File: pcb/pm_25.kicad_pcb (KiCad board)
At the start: 2 copper layers, 52.3 x 36.8 mm, 7 parts, among them J1 USB_B_Mini, U1 LD1117S33TR_TO220, U2 SI7021, U3 ESP-01v090, U4 Plantower-PM2.5

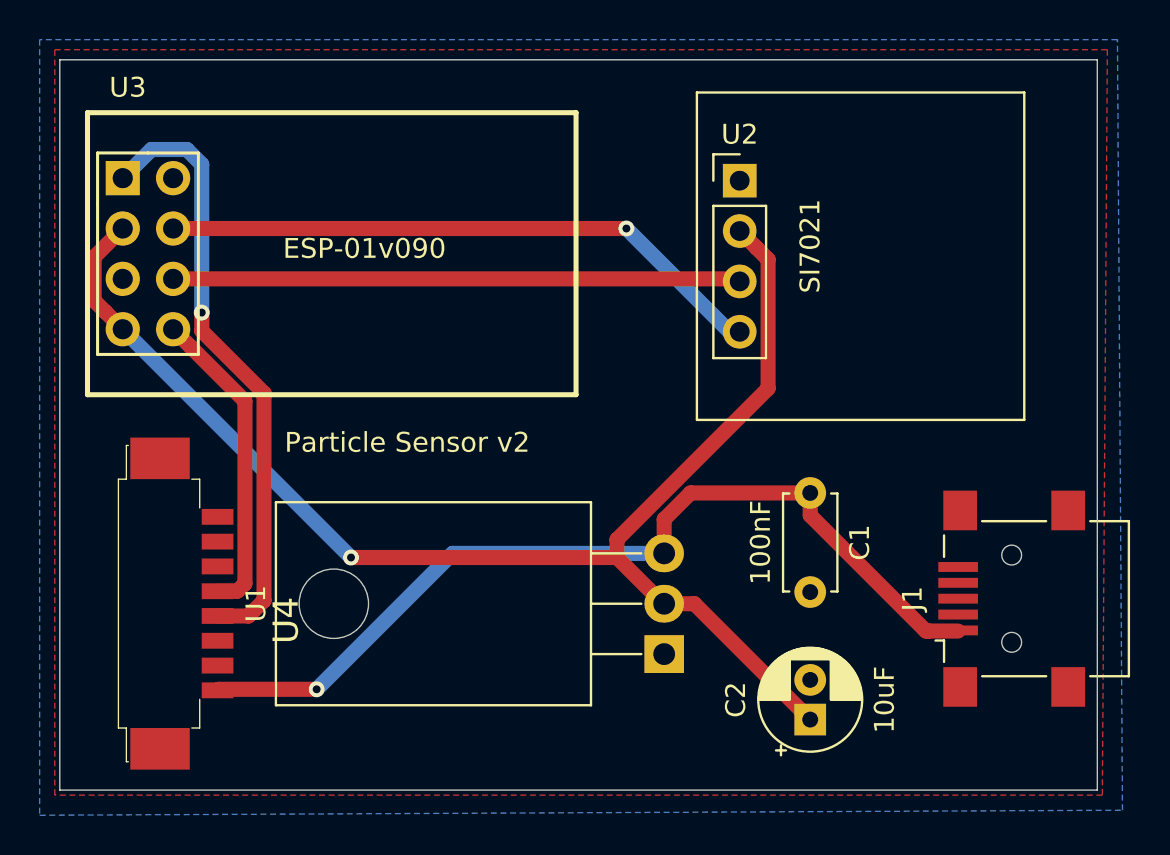
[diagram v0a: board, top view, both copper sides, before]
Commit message: make the PCB the same size as the plantower sensor
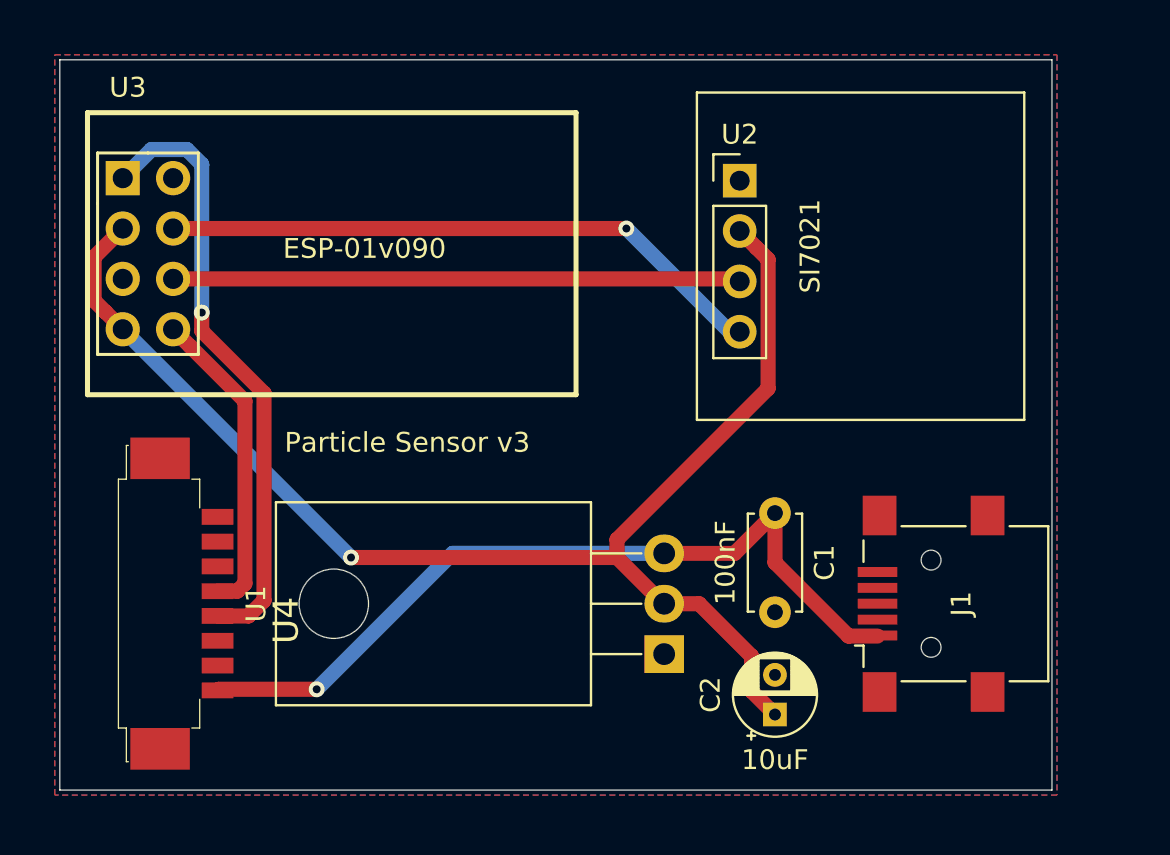
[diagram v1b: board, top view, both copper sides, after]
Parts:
- C2: footprint Capacitor_THT:CP_Radial_D5.0mm_P2.00mm -> Capacitor_THT:CP_Radial_D4.0mm_P2.00mm
- J1: value USB_B_Mini -> USB_B_Micro
- moved J1 4.07 mm to (181.1, 131.6)
- moved C1 2.05 mm to (173.2, 127.0)
- moved C2 1.80 mm to (173.2, 137.2)
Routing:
- net +5V: track 46.0 -> 41.0 mm
- net +3V3: track 69.3 -> 68.5 mm
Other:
- board size 52.3 x 36.8 mm -> 50 x 36.8 mm
- board text added: "Particle Sensor v3"
- board text removed: "Particle Sensor v2"

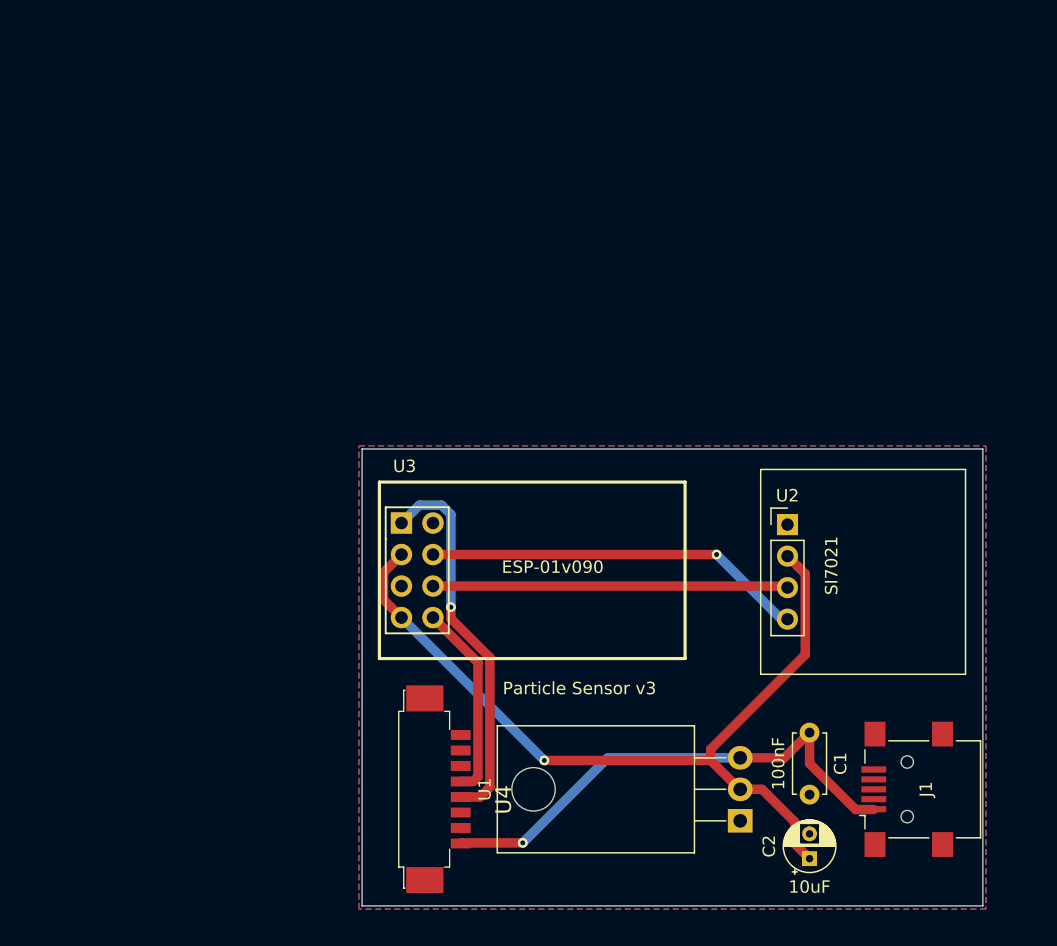
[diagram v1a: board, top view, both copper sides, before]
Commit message: updating pcb
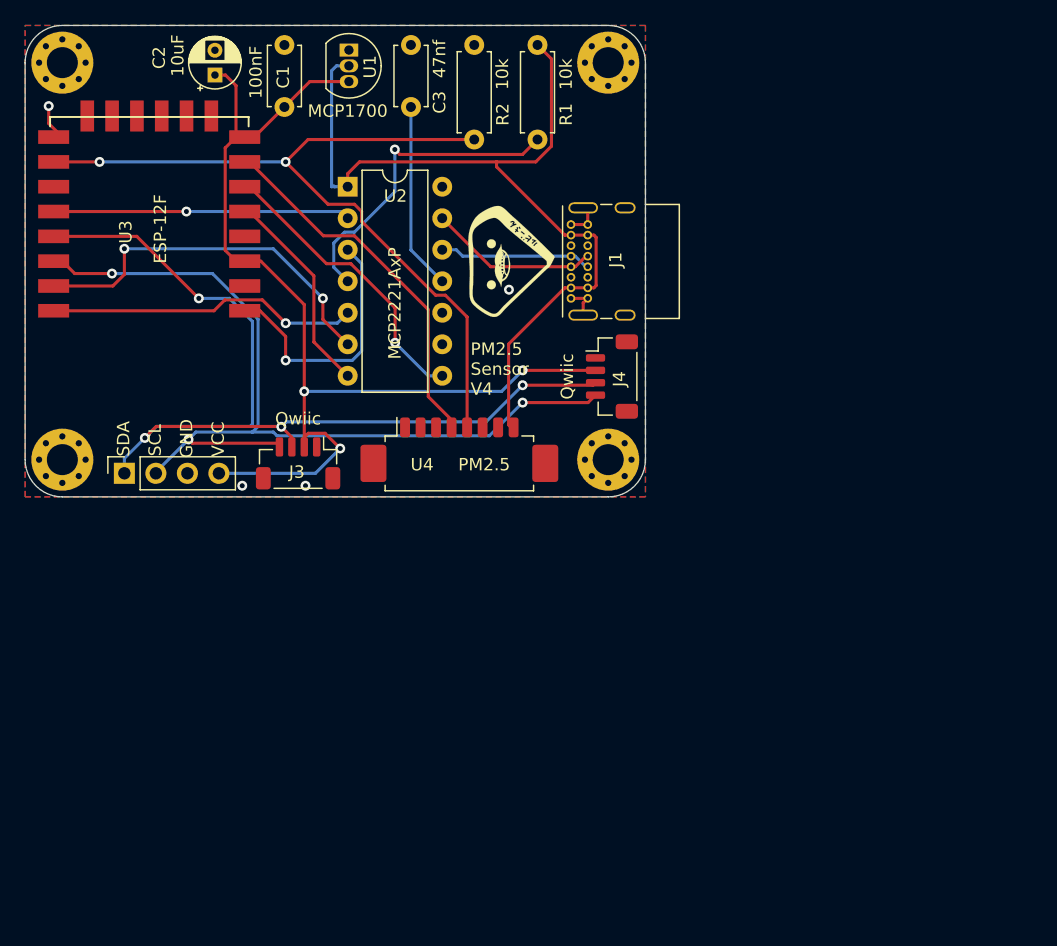
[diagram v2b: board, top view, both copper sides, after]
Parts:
- added C3: 47nf, Capacitor_THT:C_Disc_D4.7mm_W2.5mm_P5.00mm, F.Cu at (141.1, 71.6)
- added G***: LOGO, artwork:gorby, B.Cu at (122.0, 89.0)
- added G***: LOGO, artwork:rubysan, F.Cu at (149.2, 89.0)
- added H1: MountingHole, MountingHole:MountingHole_2.5mm_Pad_Via, F.Cu at (157.0, 73.0)
- added H2: MountingHole, MountingHole:MountingHole_2.5mm_Pad_Via, F.Cu at (113.0, 73.0)
- added H3: MountingHole, MountingHole:MountingHole_2.5mm_Pad_Via, F.Cu at (113.0, 105.0)
- added H4: MountingHole, MountingHole:MountingHole_2.5mm_Pad_Via, F.Cu at (157.0, 105.0)
- added J2: header, Connector_PinSocket_2.54mm:PinSocket_1x04_P2.54mm_Vertical, F.Cu at (118.0, 106.1)
- added J3: Qwiic, Connector_JST:JST_SH_BM04B-SRSS-TB_1x04-1MP_P1.00mm_Vertical, F.Cu at (132.0, 105.3)
- added J4: Qwiic, Connector_JST:JST_SH_BM04B-SRSS-TB_1x04-1MP_P1.00mm_Vertical, F.Cu at (157.3, 98.3)
- added R1: 10k, Resistor_THT:R_Axial_DIN0207_L6.3mm_D2.5mm_P7.62mm_Horizontal, F.Cu at (151.3, 71.6)
- added R2: 10k, Resistor_THT:R_Axial_DIN0207_L6.3mm_D2.5mm_P7.62mm_Horizontal, F.Cu at (146.2, 79.2)
- J1: value USB_B_Micro -> USB_C_Receptacle_USB2.0; footprint Connector_USB:USB_Mini-B_Lumberg_2486_01_Horizontal -> Connector_USB:USB_C_Receptacle_GCT_USB4085
- U1: value LD1117S33TR_TO220 -> MCP1700; footprint Package_TO_SOT_THT:TO-220-3_Horizontal_TabDown -> Package_TO_SOT_THT:TO-92_Inline
- U2: value SI7021 -> MCP2221AxP; footprint pm_25:SI7021Breakout -> Package_DIP:DIP-14_W7.62mm
- U3: value ESP-01v090 -> ESP-12F; footprint ESP8266:ESP-01 -> ESP8266:ESP-12E_SMD
- U4: value Plantower-PM2.5 -> PM2.5; footprint PMSX003-Breakout:0532610871 -> Connector_Molex:Molex_PicoBlade_53261-0871_1x08-1MP_P1.25mm_Horizontal
- moved C2 79.3 mm to (125.3, 74.0)
- moved U1 69.7 mm to (136.1, 72.0), turned to 270 degrees
- moved C1 65.8 mm to (130.9, 76.6), turned to 90 degrees
- moved U2 51.9 mm to (136.0, 83.0)
- moved J1 48.0 mm to (154.0, 92.0)
- moved U4 26.9 mm to (145.0, 104.8), turned to 0 degrees
- moved U3 21.7 mm to (127.0, 93.0), turned to 180 degrees
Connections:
- C1 pad 1: +5V -> +3V3
- U1 pad 2: +3V3 -> +5V
- U1 pad 3: +5V -> +3V3
- U2 pad 1: Net-(U2-Pad1) -> +5V
- U2 pad 2: Net-(U2-Pad2) -> /FLASH
- U2 pad 3: +3V3 -> /RST
- U2 pad 4: GND -> Net-(R1-Pad2)
- U3 pad 1: Net-(U3-Pad1) -> /RST
- U3 pad 2: GND -> (no net)
- U3 pad 4: Net-(U2-Pad1) -> (no net)
- U3 pad 5: (no net) -> Net-(U2-Pad7)
- U3 pad 6: Net-(U2-Pad2) -> Net-(U2-Pad8)
- U3 pad 7: +3V3 -> Net-(U3-Pad7)
- U3 pad 8: Net-(U3-Pad8) -> +3V3
- U4 pad 1: +5V -> (no net)
- U4 pad 2: GND -> (no net)
- U4 pad 4: Net-(U3-Pad1) -> Net-(U3-Pad7)
- U4 pad 5: Net-(U3-Pad8) -> Net-(R2-Pad1)
- U4 pad 7: (no net) -> GND
- U4 pad 8: (no net) -> +5V
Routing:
- net /SDA: track 0.00 -> 79.2 mm, vias 0 -> 4
- net /SCL: track 0.00 -> 72.7 mm, vias 0 -> 3
- net Net-(R2-Pad1): track 0.00 -> 63.4 mm, vias 0 -> 2
- net Net-(U3-Pad7): track 0.00 -> 30.9 mm
- net Net-(U3-Pad1): track 30.9 -> 0.00 mm, vias 1 -> 0
- net Net-(U2-Pad1): track 30.7 -> 0.00 mm, vias 1 -> 0
- net Net-(U2-Pad6): track 0.00 -> 29.6 mm, vias 0 -> 2
- net +5V: track 41.0 -> 70.1 mm, vias 1 -> 0
- net Net-(U2-Pad2): track 28.6 -> 0.00 mm
- net Net-(R1-Pad2): track 0.00 -> 25.8 mm, vias 0 -> 1
- net Net-(U2-Pad8): track 0.00 -> 24.6 mm, vias 0 -> 1
- net Net-(U2-Pad5): track 0.00 -> 24.5 mm, vias 0 -> 1
- net /FLASH: track 0.00 -> 23.2 mm, vias 0 -> 1
- net /RST: track 0.00 -> 21.9 mm, vias 0 -> 1
- net Net-(U2-Pad7): track 0.00 -> 17.6 mm
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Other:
- board size 50 x 36.8 mm -> 50 x 38 mm
- board text added: "GND"
- board text added: "PM2.5 Sensor V4"
- board text added: "Qwiic"
- board text added: "SCL"
- board text added: "SDA"
- board text added: "VCC"
- board text removed: "Particle Sensor v3"

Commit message: updating PCB
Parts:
- removed G***: LOGO, artwork:gorby
- removed G***: LOGO, artwork:rubysan
- J4: value Qwiic -> I2C 5v
- U3: footprint ESP8266:ESP-12E_SMD -> RF_Module:ESP-12E
- moved R1 25.2 mm to (130.6, 85.9)
- moved R2 23.8 mm to (127.2, 93.5)
- moved U2 21.5 mm to (115.2, 77.7)
- moved U1 20.9 mm to (156.2, 77.7)
- moved U3 18.5 mm to (143.0, 83.8)
- moved C3 12.0 mm to (130.6, 77.3)
- moved C1 6.84 mm to (127.2, 82.3)
- moved C2 3.07 mm to (128.3, 73.3), turned to 0 degrees
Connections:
- J4 pad 2: +3V3 -> +5V
- U3 pad 10: Net-(R2-Pad1) -> (no net)
- U3 pad 12: /FLASH -> (no net)
- U3 pad 13: /SDA -> (no net)
- U3 pad 14: /SCL -> (no net)
- U3 pad 15: Net-(U2-Pad6) -> GND
- U3 pad 16: Net-(U2-Pad5) -> Net-(R2-Pad1)
- U3 pad 18: (no net) -> /FLASH
- U3 pad 19: (no net) -> /SDA
- U3 pad 20: (no net) -> /SCL
- U3 pad 21: (no net) -> Net-(U2-Pad6)
- U3 pad 22: (no net) -> Net-(U2-Pad5)
- U3 pad 9: GND -> (no net)
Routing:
- net Net-(U2-Pad7): track 17.6 -> 85.9 mm, vias 0 -> 1
- net Net-(U2-Pad8): track 24.6 -> 65.6 mm
- net /D+: track 13.7 -> 49.6 mm
- net /RST: track 21.9 -> 50.5 mm, vias 1 -> 2
- net Net-(U2-Pad5): track 24.5 -> 52.7 mm, vias 1 -> 2
- net /D-: track 12.3 -> 35.6 mm
- net Net-(U2-Pad6): track 29.6 -> 51.0 mm, vias 2 -> 1
- net Net-(R2-Pad1): track 63.4 -> 46.0 mm, vias 2 -> 1
- net GND: track 8.66 -> 25.1 mm, vias 4 -> 6
- net Net-(U3-Pad7): track 30.9 -> 45.8 mm
- net +5V: track 70.1 -> 78.0 mm
- net /SDA: track 79.2 -> 71.6 mm, vias 4 -> 2
- net Net-(R1-Pad2): track 25.8 -> 18.8 mm, vias 1 -> 0
- net Net-(C3-Pad2): track 15.1 -> 9.01 mm
- net +3V3: track 85.1 -> 88.6 mm, vias 3 -> 1
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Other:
- board text added: "PM2.5 Sensor V4.1"
- board text removed: "PM2.5 Sensor V4"

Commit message: making it look better
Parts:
- added G***: LOGO, artwork:gorby, B.Cu at (143.4, 89.8)
- added G***: LOGO, artwork:rubysan, F.Cu at (121.1, 98.3)
- moved J4 44.8 mm to (120.5, 72.7), turned to 0 degrees
- moved C2 1.92 mm to (130.1, 72.7)
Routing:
- net /SDA: track 71.6 -> 82.7 mm, vias 2 -> 1
- net /SCL: track 71.0 -> 76.8 mm, vias 4 -> 3
- net GND: track 25.1 -> 29.7 mm
- net +5V: track 78.0 -> 82.0 mm
- net +3V3: track 88.6 -> 87.1 mm
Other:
- board text added: "I2C 3.3v"
- board text added: "PM2.5 Sensor V4.2"
- board text removed: "PM2.5 Sensor V4.1"
- board text removed: "Qwiic"

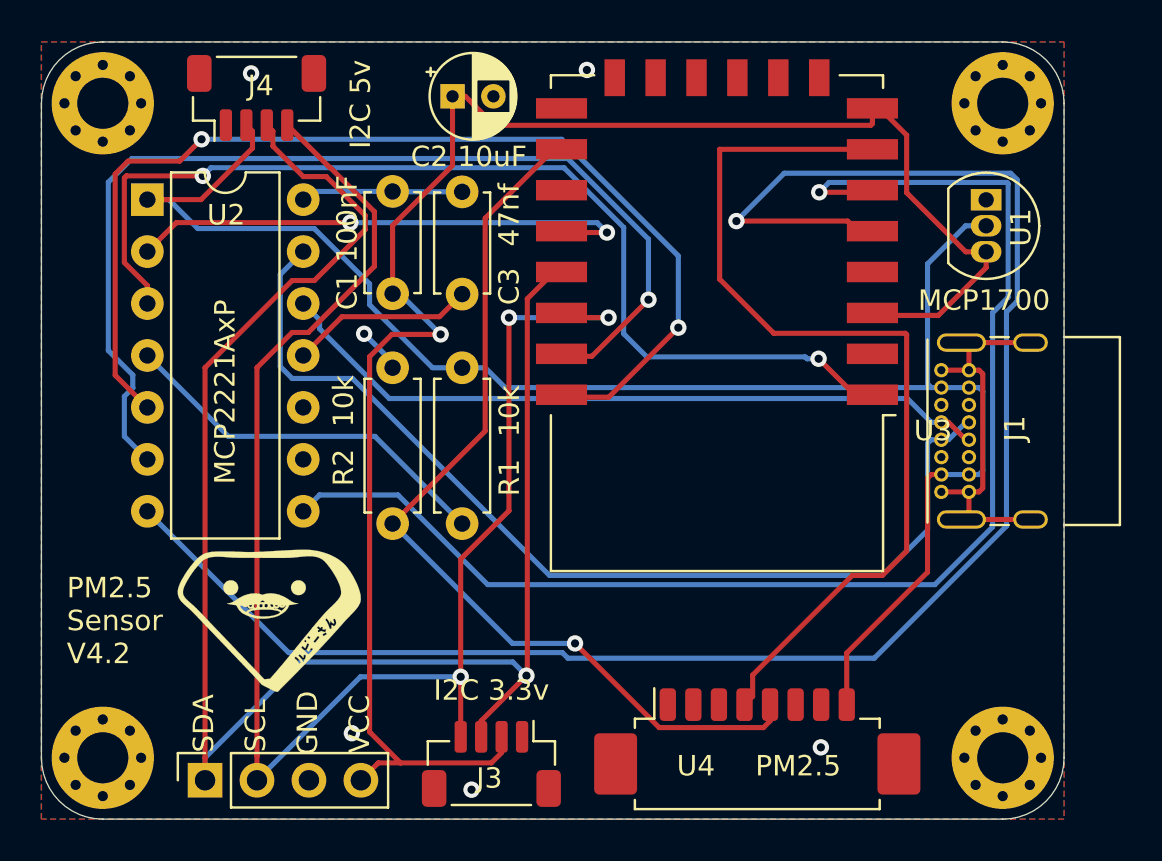
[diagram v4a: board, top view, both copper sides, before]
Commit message: update pcb with pulldown resistors for USB-C
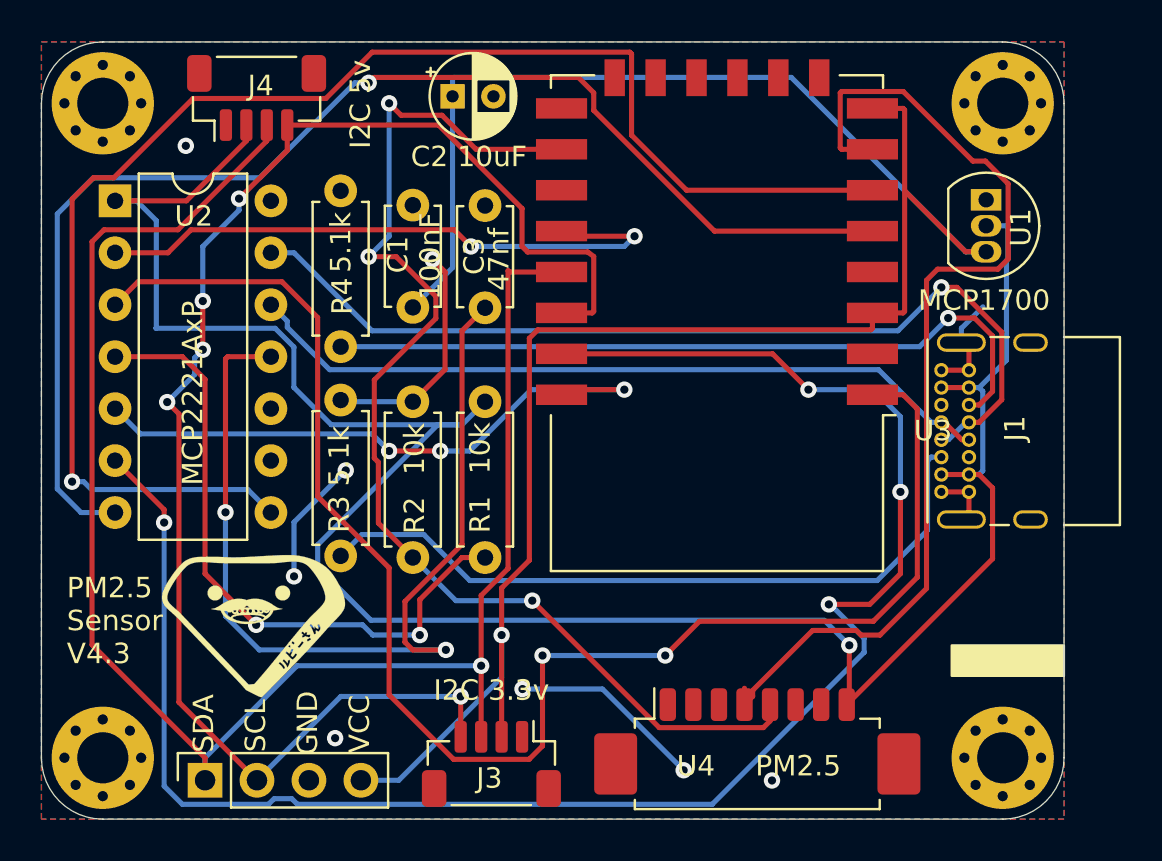
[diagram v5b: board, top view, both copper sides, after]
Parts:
- added R3: 5.1k, Resistor_THT:R_Axial_DIN0207_L6.3mm_D2.5mm_P7.62mm_Horizontal, F.Cu at (124.6, 95.1)
- added R4: 5.1k, Resistor_THT:R_Axial_DIN0207_L6.3mm_D2.5mm_P7.62mm_Horizontal, F.Cu at (124.6, 84.9)
- J3: value Qwiic -> I2C 3.3v
- moved R1 2.00 mm to (131.7, 87.6)
- moved R2 1.93 mm to (128.2, 95.2)
- moved U2 1.58 mm to (113.6, 77.8)
- moved C3 1.31 mm to (131.7, 78.0)
- moved C1 1.20 mm to (128.2, 83.0)
- moved G*** 0.86 mm to (143.8, 89.0)
- moved G*** 0.81 mm to (120.4, 98.6)
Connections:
- J1 pad A5: (no net) -> /CC1
- J1 pad B5: (no net) -> /CC2
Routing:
- net Net-(C3-Pad2): track 9.01 -> 46.4 mm, vias 0 -> 2
- net /CC2: track 0.00 -> 37.0 mm, vias 0 -> 1
- net Net-(U2-Pad6): track 51.0 -> 87.5 mm, vias 1 -> 4
- net /CC1: track 0.00 -> 35.2 mm
- net +5V: track 82.0 -> 109.5 mm, vias 0 -> 1
- net /RST: track 50.5 -> 75.1 mm
- net Net-(U2-Pad7): track 85.9 -> 63.0 mm
- net Net-(U2-Pad5): track 52.7 -> 30.2 mm, vias 2 -> 3
- net +3V3: track 87.1 -> 108.7 mm
- net Net-(R1-Pad2): track 18.8 -> 31.9 mm, vias 0 -> 2
- net Net-(R2-Pad1): track 46.0 -> 58.0 mm, vias 1 -> 3
- net Net-(U2-Pad8): track 65.6 -> 71.4 mm
- net GND: track 29.7 -> 35.1 mm, vias 6 -> 8
- net /FLASH: track 24.9 -> 30.1 mm
- net Net-(U3-Pad7): track 45.8 -> 50.0 mm
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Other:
- board text added: "PM2.5 Sensor V4.3"
- board text removed: "PM2.5 Sensor V4.2"
